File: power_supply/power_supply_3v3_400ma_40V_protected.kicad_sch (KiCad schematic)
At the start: 9 parts, among them U5 TLE42744DV33ATMA1

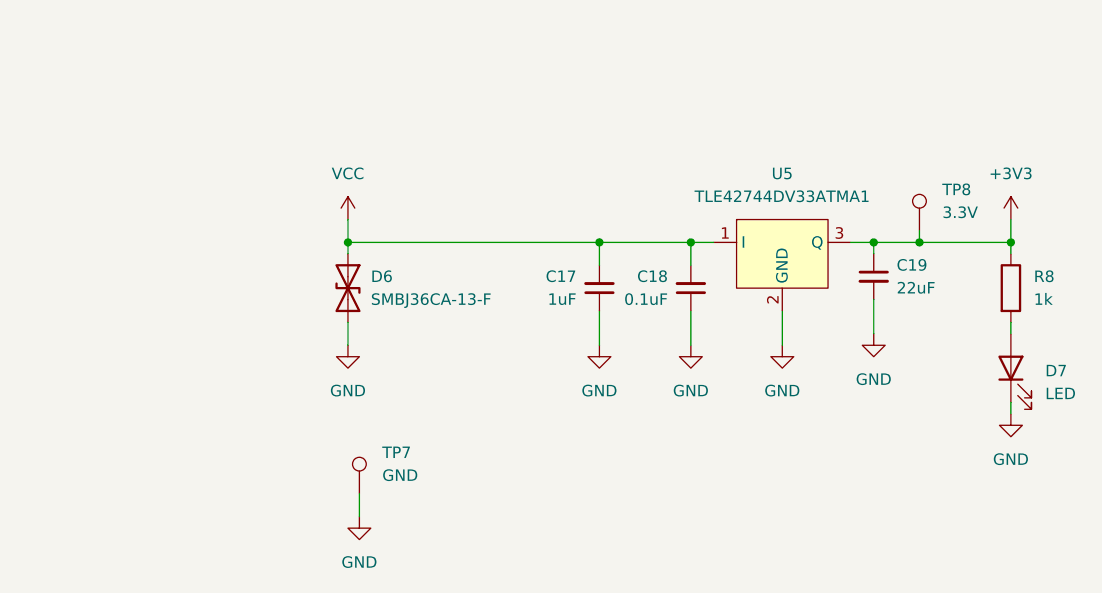
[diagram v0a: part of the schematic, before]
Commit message: added hierarchical labels
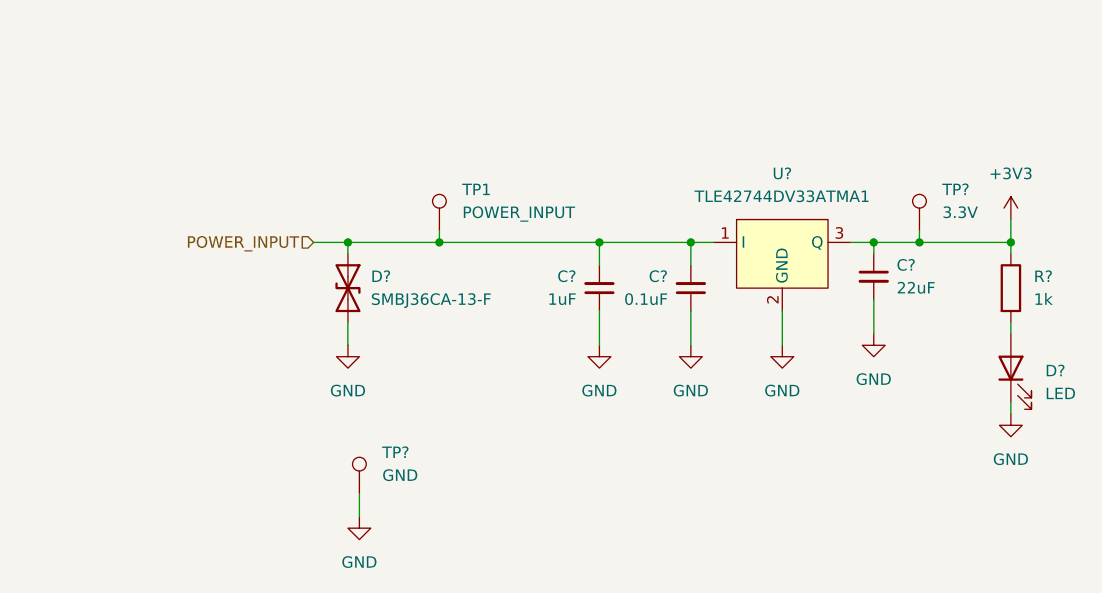
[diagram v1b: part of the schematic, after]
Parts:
- added TP1: POWER_INPUT, TestPoint:TestPoint_Pad_D2.0mm, symbol Connector:TestPoint
- renumbered C18 to C?, C17 to C?, C19 to C?, D6 to D?, D7 to D?, R8 to R?, TP8 to TP?, TP7 to TP?, U5 to U?
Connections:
- net VCC renamed POWER_INPUT
- net POWER_INPUT: now also TP1.1
